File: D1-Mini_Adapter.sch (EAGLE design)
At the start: 25 parts

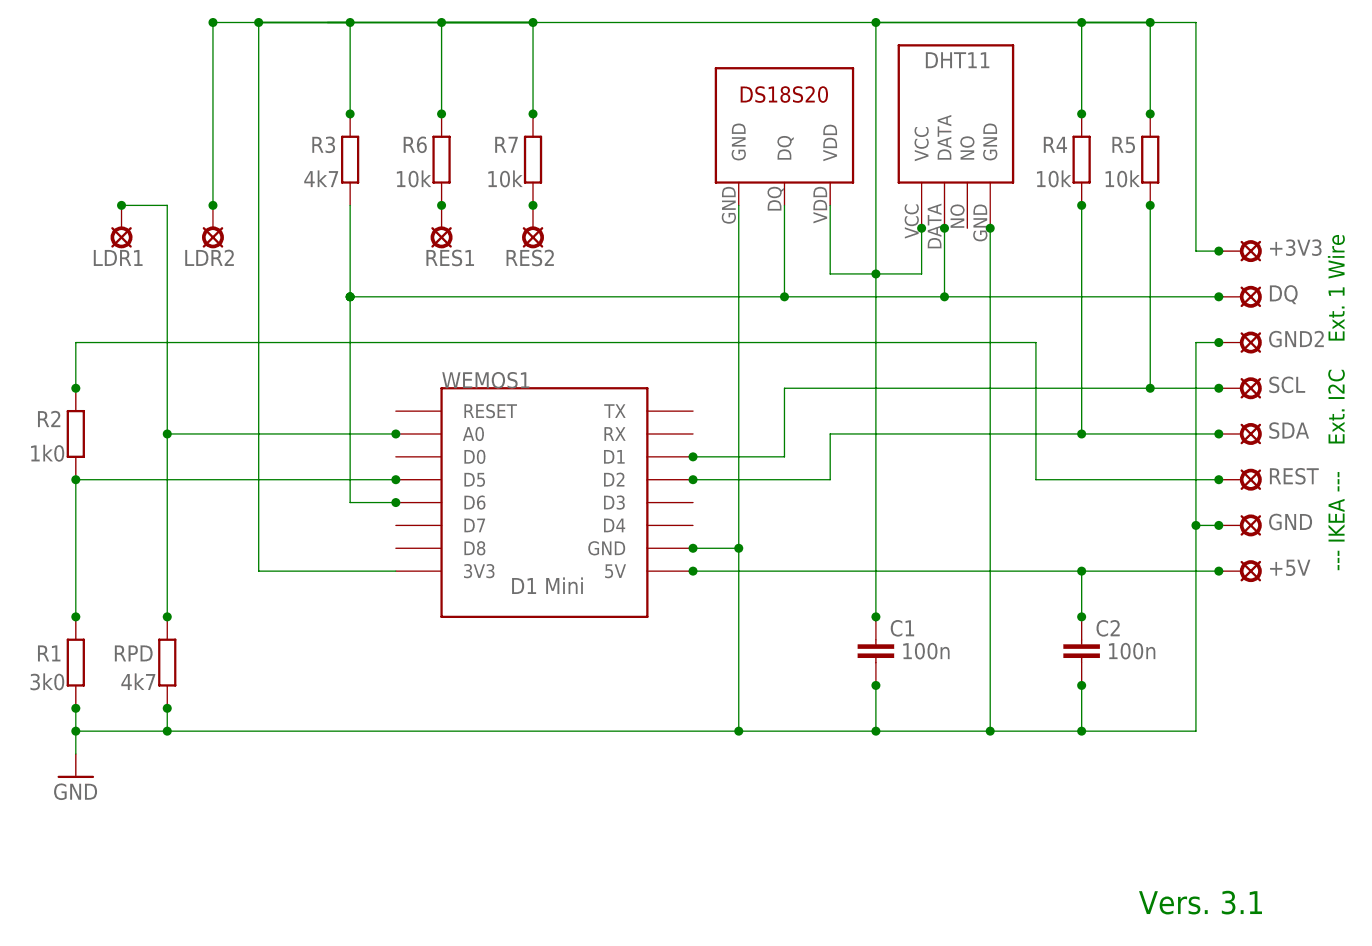
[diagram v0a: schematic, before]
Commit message: Schaltplan übersichtlicher
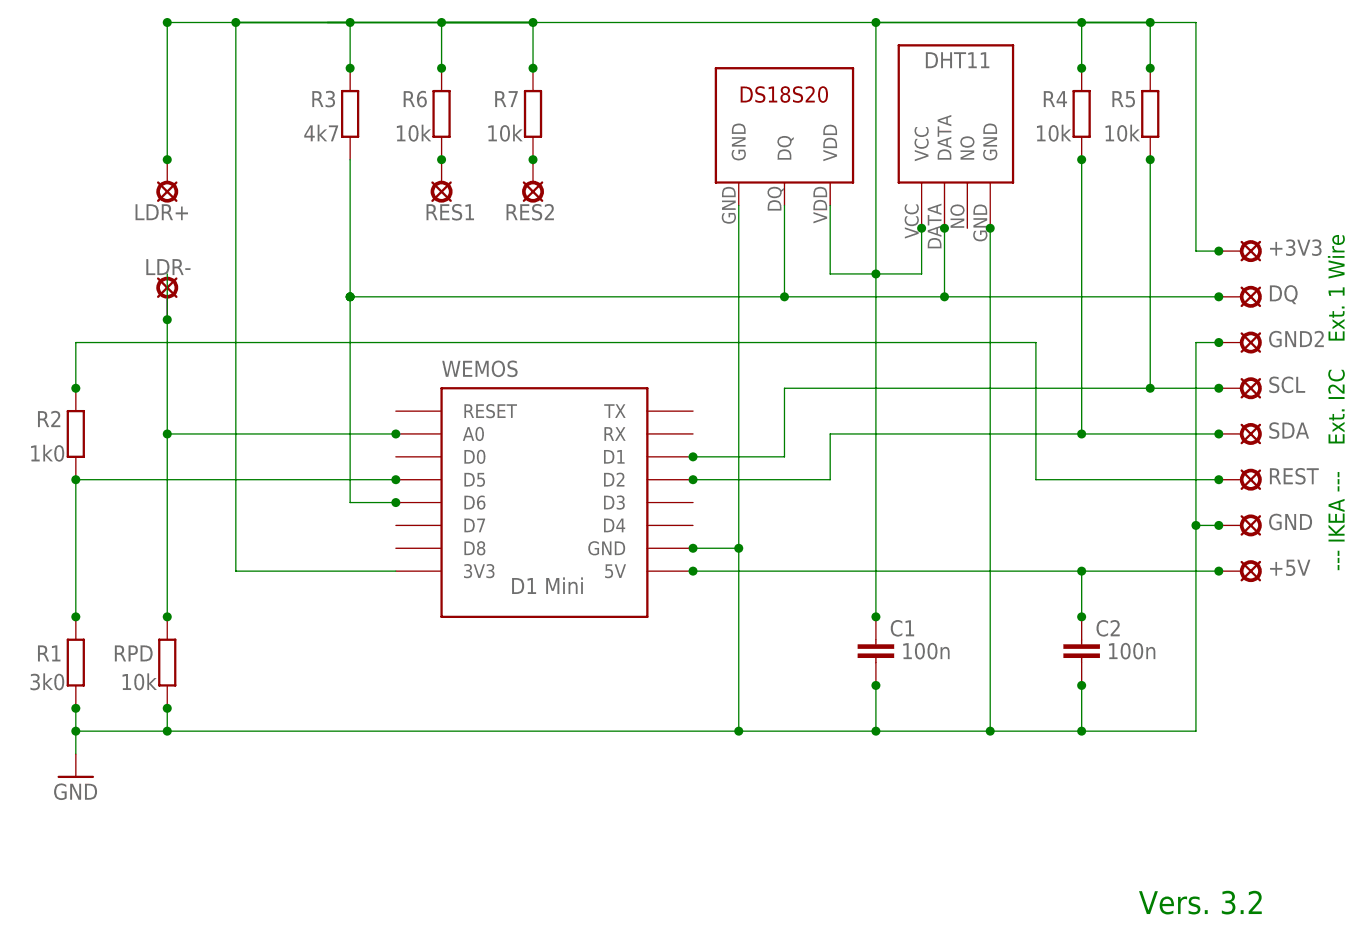
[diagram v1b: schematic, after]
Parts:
- removed LDR1, LDR2: SE13, solpad:SE13
- added LDR+, LDR-: SE13, solpad:SE13
- RPD: value 4k7 -> 10k
- renumbered WEMOS1 to WEMOS
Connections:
- net 3V3: now also LDR+.MP; no longer LDR2.MP
- net N$3: now also LDR-.MP; no longer LDR1.MP
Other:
- note added: "Vers. 3.2"
- note removed: "Vers. 3.1"
- moved on the sheet: R3, R4, R5, R6, R7, RES1, RES2
